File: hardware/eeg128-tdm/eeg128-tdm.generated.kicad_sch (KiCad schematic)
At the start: 640 parts, among them J1 0.5K-QX-32PWB, J10 S4B-PH-SM4-TB(LF)(SN), J11 S2B-PH-SM4-TB(LF)(SN), J2 0.5K-QX-32PWB, J3 0.5K-QX-32PWB, J4 0.5K-QX-32PWB, J5 0.5K-QX-32PWB, J6 0.5K-QX-32PWB, J7 0.5K-QX-32PWB, J8 0.5K-QX-32PWB, J9 TYPE-C-31-M-12, U1 CD74HC4067M96, U10 CD74HC4067M96, U11 CD74HC4067M96, U12 CD74HC4067M96, U13 CD74HC4067M96, U14 CD74HC4067M96, U15 CD74HC4067M96, U16 CD74HC4067M96, U17 TLV9064IPWR, U18 TLV9064IPWR, U19 TLV9064IPWR, U2 CD74HC4067M96, U20 TLV9064IPWR, U21 ADS131M08IPBSR, U22 OPA4171AIPWR, U23 RP2040, U24 TPS7A2033PDBVR, U25 AP2112K-3.3TRG1, U26 W25Q16JVSSIQ, U27 OT2JI-111-8.192M, U3 CD74HC4067M96, U4 CD74HC4067M96, U5 CD74HC4067M96, U6 CD74HC4067M96, U7 CD74HC4067M96, U8 CD74HC4067M96, U9 CD74HC4067M96, Y1 X322512MSB4SI

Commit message: Materialize generated KiCad schematic and release manifest
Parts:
- added R538: 0603WAF5101T5E, NBFM1_A0:R538, symbol NBFM1_A0:GEN_2_a2422ced9e0c
- added R539: 0603WAF5101T5E, NBFM1_A0:R539, symbol NBFM1_A0:GEN_2_a2422ced9e0c
- J9: symbol NBFM1_A0:GEN_18_30158393f200 -> NBFM1_A0:GEN_20_6661cee1473b
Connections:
- net DGND is gone; now on net AGND: C61.1 (Pin_1), C63.1 (Pin_1), C64.1 (Pin_1), U21.8 (Pin_8), U23.1 (Pin_1), U26.5 (Pin_5), U27.3 (Pin_3)
- net ISO_GND is gone; now on net AGND: J11.1 (Pin_1)
- net VCM_DIV_HI is gone; now on net 3V3A: R529.2 (Pin_2)
- net 3V3A: now also C1.2 (Pin_2), C10.2 (Pin_2), C11.2 (Pin_2), C12.2 (Pin_2), C13.2 (Pin_2), C14.2 (Pin_2), C15.2 (Pin_2), C16.2 (Pin_2), C18.2 (Pin_2), C2.2 (Pin_2), C21.2 (Pin_2), C22.2 (Pin_2), C23.2 (Pin_2), C24.2 (Pin_2), C25.2 (Pin_2), C26.2 (Pin_2), C27.2 (Pin_2), C28.2 (Pin_2), C29.2 (Pin_2), C3.2 (Pin_2), C30.2 (Pin_2), C31.2 (Pin_2), C32.2 (Pin_2), C33.2 (Pin_2), C34.2 (Pin_2), C35.2 (Pin_2), C36.2 (Pin_2), C37.2 (Pin_2), C38.2 (Pin_2), C39.2 (Pin_2), C4.2 (Pin_2), C40.2 (Pin_2), C41.2 (Pin_2), C5.2 (Pin_2), C6.2 (Pin_2), C7.2 (Pin_2), C8.2 (Pin_2), C9.2 (Pin_2), U24.1 (Pin_1)
- net 3V3D: now also C20.2 (Pin_2), C42.2 (Pin_2), C44.2 (Pin_2), C45.2 (Pin_2), C46.2 (Pin_2), C47.2 (Pin_2), C48.2 (Pin_2), C49.2 (Pin_2), C53.2 (Pin_2), C54.2 (Pin_2), C55.2 (Pin_2), C56.2 (Pin_2), C57.2 (Pin_2), C58.2 (Pin_2), C59.2 (Pin_2), C60.2 (Pin_2), U25.1 (Pin_1), U27.4 (Pin_4)
- net 5V_ISO: now also C17.2 (Pin_2), C19.2 (Pin_2), J9.A6 (Pin_A6), J9.B12 (Pin_B12), J9.B6 (Pin_B6), J9.S1 (Pin_S1), U24.3 (Pin_3), U24.5 (Pin_5), U25.3 (Pin_3), U25.5 (Pin_5)
- net ADC_REFIN: now also C43.2 (Pin_2)
- net AGND: now also C1.1 (Pin_1), C10.1 (Pin_1), C11.1 (Pin_1), C12.1 (Pin_1), C13.1 (Pin_1), C14.1 (Pin_1), C15.1 (Pin_1), C16.1 (Pin_1), C17.1 (Pin_1), C18.1 (Pin_1), C19.1 (Pin_1), C2.1 (Pin_1), C20.1 (Pin_1), C21.1 (Pin_1), C22.1 (Pin_1), C23.1 (Pin_1), C24.1 (Pin_1), C25.1 (Pin_1), C26.1 (Pin_1), C27.1 (Pin_1), C28.1 (Pin_1), C29.1 (Pin_1), C3.1 (Pin_1), C30.1 (Pin_1), C31.1 (Pin_1), C32.1 (Pin_1), C33.1 (Pin_1), C34.1 (Pin_1), C35.1 (Pin_1), C36.1 (Pin_1), C37.1 (Pin_1), C38.1 (Pin_1), C39.1 (Pin_1), C4.1 (Pin_1), C40.1 (Pin_1), C41.1 (Pin_1), C42.1 (Pin_1), C43.1 (Pin_1), C44.1 (Pin_1), C45.1 (Pin_1), C46.1 (Pin_1), C47.1 (Pin_1), C48.1 (Pin_1), C49.1 (Pin_1), C5.1 (Pin_1), C50.1 (Pin_1), C51.1 (Pin_1), C52.1 (Pin_1), C53.1 (Pin_1), C54.1 (Pin_1), C55.1 (Pin_1), C56.1 (Pin_1), C57.1 (Pin_1), C58.1 (Pin_1), C59.1 (Pin_1), C6.1 (Pin_1), C60.1 (Pin_1), C7.1 (Pin_1), C8.1 (Pin_1), C9.1 (Pin_1), J9.B4 (Pin_B4), J9.B5 (Pin_B5), J9.S1 (Pin_S1), U24.4 (Pin_4), U25.4 (Pin_4), Y1.1 (Pin_1), Y1.3 (Pin_3), R538.1 (Pin_1), R539.1 (Pin_1)
- net SHIELD: now also J9.A5 (Pin_A5)
- net USB_DM: now also J9.A8 (Pin_A8), J9.B8 (Pin_B8)
- net USB_DP: now also J9.A9 (Pin_A9), J9.B9 (Pin_B9)
- net VREG_1V1: now also C50.2 (Pin_2), C51.2 (Pin_2), C52.2 (Pin_2)
- new net USB_CC1: J9.S1 (Pin_S1), R538.2 (Pin_2)
- new net USB_CC2: J9.B1 (Pin_B1), R539.2 (Pin_2)
- no-connect marks 176 -> 32

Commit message: Materialize generated KiCad schematic and release manifest
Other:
- moved on the sheet: C10, C13, C14, C15, C18, C19, C20, C23, C24, C28, C29, C3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

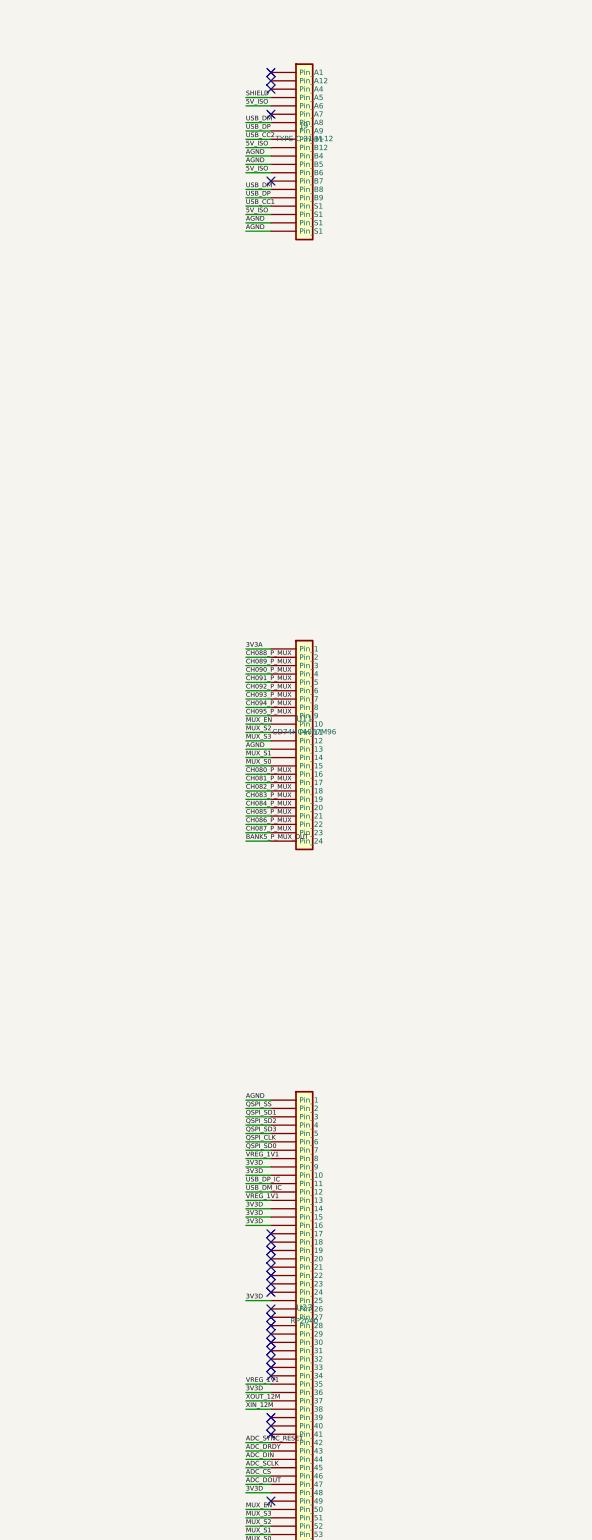
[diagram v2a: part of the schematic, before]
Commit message: Materialize generated KiCad schematic and release manifest
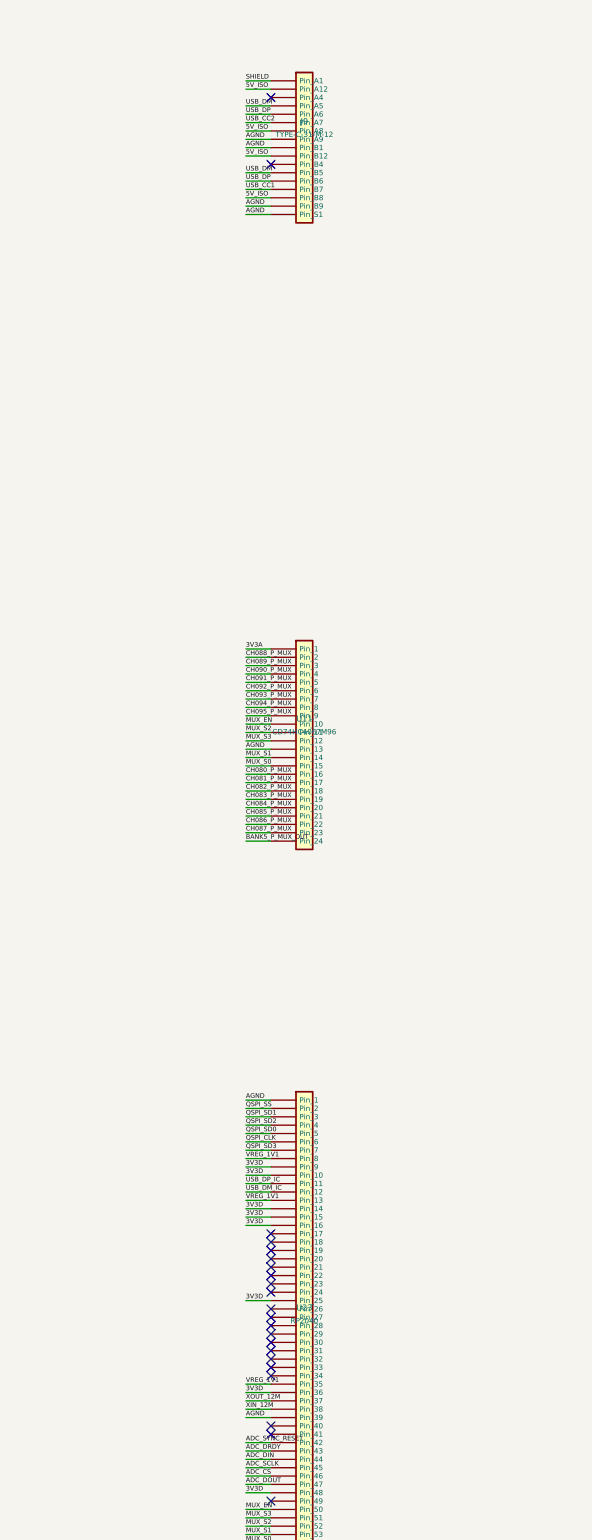
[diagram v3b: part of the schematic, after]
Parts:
- J9: symbol NBFM1_A0:GEN_20_6661cee1473b -> NBFM1_A0:GEN_17_9492c1d87d9b
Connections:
- net 5V_ISO: now also J9.A12 (Pin_A12), J9.A8 (Pin_A8), J9.B8 (Pin_B8); no longer J9.A6 (Pin_A6), J9.B6 (Pin_B6), J9.S1 (Pin_S1)
- net AGND: now also J9.A9 (Pin_A9), J9.B1 (Pin_B1), J9.B9 (Pin_B9), U23.39 (Pin_39); no longer J9.B4 (Pin_B4), J9.B5 (Pin_B5)
- net QSPI_SD0: now also U23.5 (Pin_5); no longer U23.7 (Pin_7)
- net QSPI_SD3: now also U23.7 (Pin_7); no longer U23.5 (Pin_5)
- net SHIELD: now also J9.A1 (Pin_A1); no longer J9.A5 (Pin_A5)
- net USB_CC1: now also J9.B7 (Pin_B7); no longer J9.S1 (Pin_S1)
- net USB_CC2: now also J9.A7 (Pin_A7); no longer J9.B1 (Pin_B1)
- net USB_DM: now also J9.A5 (Pin_A5), J9.B5 (Pin_B5); no longer J9.A8 (Pin_A8), J9.B8 (Pin_B8)
- net USB_DP: now also J9.A6 (Pin_A6), J9.B6 (Pin_B6); no longer J9.A9 (Pin_A9), J9.B9 (Pin_B9)
- no-connect marks 32 -> 28
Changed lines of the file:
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@@
   )
   (wire
-    (pts (xy 775.970 67.310) (xy 772.160 67.310))
-    (stroke (width 0) (type default))
-  )
-  (wire
-    (pts (xy 775.970 66.040) (xy 772.160 66.040))
-    (stroke (width 0) (type default))
-  )
-  (wire
     (pts (xy 775.970 64.770) (xy 772.160 64.770))
     (stroke (width 0) (type default))
@@
   )
   (wire
-    (pts (xy 775.970 58.420) (xy 772.160 58.420))
+    (pts (xy 775.970 59.690) (xy 772.160 59.690))
     (stroke (width 0) (type default))
   )
   (wire
-    (pts (xy 775.970 57.150) (xy 772.160 57.150))
+    (pts (xy 775.970 58.420) (xy 772.160 58.420))
     (stroke (width 0) (type default))
   )
@@
   )
   (wire
+    (pts (xy 775.970 49.530) (xy 772.160 49.530))
+    (stroke (width 0) (type default))
+  )
+  (wire
     (pts (xy 775.970 48.260) (xy 772.160 48.260))
     (stroke (width 0) (type default))
   )
   (wire
-    (pts (xy 775.970 46.990) (xy 772.160 46.990))
+    (pts (xy 775.970 45.720) (xy 772.160 45.720))
+    (stroke (width 0) (type default))
+  )
+  (wire
+    (pts (xy 775.970 44.450) (xy 772.160 44.450))
     (stroke (width 0) (type default))
   )
@@
   )
   (wire
+    (pts (xy 775.970 247.650) (xy 772.160 247.650))
+    (stroke (width 0) (type default))
+  )
+  (wire
     (pts (xy 775.970 246.380) (xy 772.160 246.380))
     (stroke (width 0) (type default))
@@
   )
   (label "AGND"
-    (at 772.160 67.310 0)
+    (at 772.160 64.770 0)
     (effects (font (size 0.7 0.7)) (justify left bottom))
   )
   (label "AGND"
-    (at 772.160 66.040 0)
+    (at 772.160 63.500 0)
     (effects (font (size 0.7 0.7)) (justify left bottom))
   )
   (label "5V_ISO"
-    (at 772.160 64.770 0)
+    (at 772.160 62.230 0)
     (effects (font (size 0.7 0.7)) (justify left bottom))
   )
   (label "USB_CC1"
-    (at 772.160 63.500 0)
+    (at 772.160 60.960 0)
     (effects (font (size 0.7 0.7)) (justify left bottom))
   )
   (label "USB_DP"
-    (at 772.160 62.230 0)
+    (at 772.160 59.690 0)
     (effects (font (size 0.7 0.7)) (justify left bottom))
   )
   (label "USB_DM"
-    (at 772.160 60.960 0)
+    (at 772.160 58.420 0)
     (effects (font (size 0.7 0.7)) (justify left bottom))
   )
   (label "5V_ISO"
-    (at 772.160 58.420 0)
+    (at 772.160 55.880 0)
     (effects (font (size 0.7 0.7)) (justify left bottom))
   )
   (label "AGND"
-    (at 772.160 57.150 0)
+    (at 772.160 54.610 0)
     (effects (font (size 0.7 0.7)) (justify left bottom))
   )
   (label "AGND"
-    (at 772.160 55.880 0)
+    (at 772.160 53.340 0)
     (effects (font (size 0.7 0.7)) (justify left bottom))
   )
   (label "5V_ISO"
-    (at 772.160 54.610 0)
+    (at 772.160 52.070 0)
     (effects (font (size 0.7 0.7)) (justify left bottom))
   )
   (label "USB_CC2"
-    (at 772.160 53.340 0)
+    (at 772.160 50.800 0)
     (effects (font (size 0.7 0.7)) (justify left bottom))
   )
   (label "USB_DP"
-    (at 772.160 52.070 0)
+    (at 772.160 49.530 0)
     (effects (font (size 0.7 0.7)) (justify left bottom))
   )
   (label "USB_DM"
-    (at 772.160 50.800 0)
+    (at 772.160 48.260 0)
     (effects (font (size 0.7 0.7)) (justify left bottom))
   )
   (label "5V_ISO"
-    (at 772.160 48.260 0)
+    (at 772.160 45.720 0)
     (effects (font (size 0.7 0.7)) (justify left bottom))
   )
   (label "SHIELD"
-    (at 772.160 46.990 0)
+    (at 772.160 44.450 0)
     (effects (font (size 0.7 0.7)) (justify left bottom))
   )
@@
     (effects (font (size 0.7 0.7)) (justify left bottom))
   )
+  (label "AGND"
+    (at 772.160 247.650 0)
+    (effects (font (size 0.7 0.7)) (justify left bottom))
+  )
   (label "XIN_12M"
     (at 772.160 246.380 0)
@@
     (effects (font (size 0.7 0.7)) (justify left bottom))
   )
-  (label "QSPI_SD0"
+  (label "QSPI_SD3"
     (at 772.160 207.010 0)
     (effects (font (size 0.7 0.7)) (justify left bottom))
@@
     (effects (font (size 0.7 0.7)) (justify left bottom))
   )
-  (label "QSPI_SD3"
+  (label "QSPI_SD0"
     (at 772.160 204.470 0)
     (effects (font (size 0.7 0.7)) (justify left bottom))
@@
     (effects (font (size 0.7 0.7)) (justify left bottom))
   )
-  (no_connect (at 775.970 59.690))
-  (no_connect (at 775.970 49.530))
-  (no_connect (at 775.970 45.720))
-  (no_connect (at 775.970 44.450))
-  (no_connect (at 775.970 43.180))
+  (no_connect (at 775.970 57.150))
+  (no_connect (at 775.970 46.990))
   (no_connect (at 591.820 228.600))
   (no_connect (at 591.820 222.250))
@@
   (no_connect (at 775.970 250.190))
   (no_connect (at 775.970 248.920))
-  (no_connect (at 775.970 247.650))
   (no_connect (at 775.970 241.300))
   (no_connect (at 775.970 240.030))
@@
   )
   (symbol
-    (lib_id "NBFM1_A0:GEN_20_6661cee1473b")
-    (at 781.050 55.245 0)
+    (lib_id "NBFM1_A0:GEN_17_9492c1d87d9b")
+    (at 781.050 54.610 0)
     (unit 1)
     (exclude_from_sim no)
@@
     (on_board yes)
     (dnp no)
-    (property "Reference" "J9" (at 781.050 51.245 0) (effects (font (size 0.9 0.9))))
-    (property "Value" "TYPE-C-31-M-12" (at 781.050 53.245 0) (effects (font (size 0.8 0.8))))
-    (property "Footprint" "NBFM1_A0:J9" (at 781.050 55.245 0) (effects (font (size 0.8 0.8)) (hide yes)))
-    (property "Datasheet" "" (at 781.050 55.245 0) (effects (font (size 0.8 0.8)) (hide yes)))
-    (property "Description" "Generated connectivity symbol; BOM footprint: USB-C-16P_RA" (at 781.050 55.245 0) (effects (font (size 0.8 0.8)) (hide yes)))
+    (property "Reference" "J9" (at 781.050 50.610 0) (effects (font (size 0.9 0.9))))
+    (property "Value" "TYPE-C-31-M-12" (at 781.050 52.610 0) (effects (font (size 0.8 0.8))))
+    (property "Footprint" "NBFM1_A0:J9" (at 781.050 54.610 0) (effects (font (size 0.8 0.8)) (hide yes)))
+    (property "Datasheet" "" (at 781.050 54.610 0) (effects (font (size 0.8 0.8)) (hide yes)))
+    (property "Description" "Generated connectivity symbol; BOM footprint: USB-C-16P_RA" (at 781.050 54.610 0) (effects (font (size 0.8 0.8)) (hide yes)))
     (pin "A1"
     )
@@
     )
     (pin "S1"
-    )
-    (pin "S1"
-    )
-    (pin "S1"
-    )
-    (pin "S1"

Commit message: Materialize generated KiCad schematic and release manifest
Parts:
- C1: footprint NBFM1_A0:C1 -> C1
- C10: footprint NBFM1_A0:C10 -> C10
- C11: footprint NBFM1_A0:C11 -> C11
- C12: footprint NBFM1_A0:C12 -> C12
- C13: footprint NBFM1_A0:C13 -> C13
- C14: footprint NBFM1_A0:C14 -> C14
- C15: footprint NBFM1_A0:C15 -> C15
- C16: footprint NBFM1_A0:C16 -> C16
- C17: footprint NBFM1_A0:C17 -> C17
- C18: footprint NBFM1_A0:C18 -> C18
- C19: footprint NBFM1_A0:C19 -> C19
- C2: footprint NBFM1_A0:C2 -> C2
- C20: footprint NBFM1_A0:C20 -> C20
- C21: footprint NBFM1_A0:C21 -> C21
- C22: footprint NBFM1_A0:C22 -> C22
- C23: footprint NBFM1_A0:C23 -> C23
- C24: footprint NBFM1_A0:C24 -> C24
- C25: footprint NBFM1_A0:C25 -> C25
- C26: footprint NBFM1_A0:C26 -> C26
- C27: footprint NBFM1_A0:C27 -> C27
- C28: footprint NBFM1_A0:C28 -> C28
- C29: footprint NBFM1_A0:C29 -> C29
- C3: footprint NBFM1_A0:C3 -> C3
- C30: footprint NBFM1_A0:C30 -> C30
- C31: footprint NBFM1_A0:C31 -> C31
- C32: footprint NBFM1_A0:C32 -> C32
- C33: footprint NBFM1_A0:C33 -> C33
- C34: footprint NBFM1_A0:C34 -> C34
- C35: footprint NBFM1_A0:C35 -> C35
- C36: footprint NBFM1_A0:C36 -> C36
- C37: footprint NBFM1_A0:C37 -> C37
- C38: footprint NBFM1_A0:C38 -> C38
- C39: footprint NBFM1_A0:C39 -> C39
- C4: footprint NBFM1_A0:C4 -> C4
- C40: footprint NBFM1_A0:C40 -> C40
- C41: footprint NBFM1_A0:C41 -> C41
- C42: footprint NBFM1_A0:C42 -> C42
- C43: footprint NBFM1_A0:C43 -> C43
- C44: footprint NBFM1_A0:C44 -> C44
- C45: footprint NBFM1_A0:C45 -> C45
- C46: footprint NBFM1_A0:C46 -> C46
- C47: footprint NBFM1_A0:C47 -> C47
- C48: footprint NBFM1_A0:C48 -> C48
- C49: footprint NBFM1_A0:C49 -> C49
- C5: footprint NBFM1_A0:C5 -> C5
- C50: footprint NBFM1_A0:C50 -> C50
- C51: footprint NBFM1_A0:C51 -> C51
- C52: footprint NBFM1_A0:C52 -> C52
- C53: footprint NBFM1_A0:C53 -> C53
- C54: footprint NBFM1_A0:C54 -> C54
- C55: footprint NBFM1_A0:C55 -> C55
- C56: footprint NBFM1_A0:C56 -> C56
- C57: footprint NBFM1_A0:C57 -> C57
- C58: footprint NBFM1_A0:C58 -> C58
- C59: footprint NBFM1_A0:C59 -> C59
- C6: footprint NBFM1_A0:C6 -> C6
- C60: footprint NBFM1_A0:C60 -> C60
- C61: footprint NBFM1_A0:C61 -> C61
- C62: footprint NBFM1_A0:C62 -> C62
- C63: footprint NBFM1_A0:C63 -> C63
- C64: footprint NBFM1_A0:C64 -> C64
- C7: footprint NBFM1_A0:C7 -> C7
- C8: footprint NBFM1_A0:C8 -> C8
- C9: footprint NBFM1_A0:C9 -> C9
- J1: footprint NBFM1_A0:J1 -> J1
- J10: footprint NBFM1_A0:J10 -> J10
- J11: footprint NBFM1_A0:J11 -> J11
- J2: footprint NBFM1_A0:J2 -> J2
- J3: footprint NBFM1_A0:J3 -> J3
- J4: footprint NBFM1_A0:J4 -> J4
- J5: footprint NBFM1_A0:J5 -> J5
- J6: footprint NBFM1_A0:J6 -> J6
- J7: footprint NBFM1_A0:J7 -> J7
- J8: footprint NBFM1_A0:J8 -> J8
- J9: footprint NBFM1_A0:J9 -> USB_C_Receptacle_HRO_TYPE-C-31-M-12
- R1: footprint NBFM1_A0:R1 -> R1
- R10: footprint NBFM1_A0:R10 -> R10
- R100: footprint NBFM1_A0:R100 -> R100
- R101: footprint NBFM1_A0:R101 -> R101
- R102: footprint NBFM1_A0:R102 -> R102
- R103: footprint NBFM1_A0:R103 -> R103
- R104: footprint NBFM1_A0:R104 -> R104
- R105: footprint NBFM1_A0:R105 -> R105
- R106: footprint NBFM1_A0:R106 -> R106
- R107: footprint NBFM1_A0:R107 -> R107
- R108: footprint NBFM1_A0:R108 -> R108
- R109: footprint NBFM1_A0:R109 -> R109
- R11: footprint NBFM1_A0:R11 -> R11
- R110: footprint NBFM1_A0:R110 -> R110
- R111: footprint NBFM1_A0:R111 -> R111
- R112: footprint NBFM1_A0:R112 -> R112
- R113: footprint NBFM1_A0:R113 -> R113
- R114: footprint NBFM1_A0:R114 -> R114
- R115: footprint NBFM1_A0:R115 -> R115
- R116: footprint NBFM1_A0:R116 -> R116
- R117: footprint NBFM1_A0:R117 -> R117
- R118: footprint NBFM1_A0:R118 -> R118
- R119: footprint NBFM1_A0:R119 -> R119
- R12: footprint NBFM1_A0:R12 -> R12
- R120: footprint NBFM1_A0:R120 -> R120
- R121: footprint NBFM1_A0:R121 -> R121
- R122: footprint NBFM1_A0:R122 -> R122
- R123: footprint NBFM1_A0:R123 -> R123
- R124: footprint NBFM1_A0:R124 -> R124
- R125: footprint NBFM1_A0:R125 -> R125
- R126: footprint NBFM1_A0:R126 -> R126
- R127: footprint NBFM1_A0:R127 -> R127
- R128: footprint NBFM1_A0:R128 -> R128
- R129: footprint NBFM1_A0:R129 -> R129
- R13: footprint NBFM1_A0:R13 -> R13
- R130: footprint NBFM1_A0:R130 -> R130
- R131: footprint NBFM1_A0:R131 -> R131
- R132: footprint NBFM1_A0:R132 -> R132
- R133: footprint NBFM1_A0:R133 -> R133
- R134: footprint NBFM1_A0:R134 -> R134
- R135: footprint NBFM1_A0:R135 -> R135
- R136: footprint NBFM1_A0:R136 -> R136
- R137: footprint NBFM1_A0:R137 -> R137
- R138: footprint NBFM1_A0:R138 -> R138
- R139: footprint NBFM1_A0:R139 -> R139
- R14: footprint NBFM1_A0:R14 -> R14
- R140: footprint NBFM1_A0:R140 -> R140
- R141: footprint NBFM1_A0:R141 -> R141
- R142: footprint NBFM1_A0:R142 -> R142
- R143: footprint NBFM1_A0:R143 -> R143
- R144: footprint NBFM1_A0:R144 -> R144
- R145: footprint NBFM1_A0:R145 -> R145
- R146: footprint NBFM1_A0:R146 -> R146
- R147: footprint NBFM1_A0:R147 -> R147
- R148: footprint NBFM1_A0:R148 -> R148
- R149: footprint NBFM1_A0:R149 -> R149
- R15: footprint NBFM1_A0:R15 -> R15
- R150: footprint NBFM1_A0:R150 -> R150
- R151: footprint NBFM1_A0:R151 -> R151
- R152: footprint NBFM1_A0:R152 -> R152
- R153: footprint NBFM1_A0:R153 -> R153
- R154: footprint NBFM1_A0:R154 -> R154
- R155: footprint NBFM1_A0:R155 -> R155
- R156: footprint NBFM1_A0:R156 -> R156
- R157: footprint NBFM1_A0:R157 -> R157
- R158: footprint NBFM1_A0:R158 -> R158
- R159: footprint NBFM1_A0:R159 -> R159
- R16: footprint NBFM1_A0:R16 -> R16
- R160: footprint NBFM1_A0:R160 -> R160
- R161: footprint NBFM1_A0:R161 -> R161
- R162: footprint NBFM1_A0:R162 -> R162
- R163: footprint NBFM1_A0:R163 -> R163
- R164: footprint NBFM1_A0:R164 -> R164
- R165: footprint NBFM1_A0:R165 -> R165
- R166: footprint NBFM1_A0:R166 -> R166
- R167: footprint NBFM1_A0:R167 -> R167
- R168: footprint NBFM1_A0:R168 -> R168
- R169: footprint NBFM1_A0:R169 -> R169
- R17: footprint NBFM1_A0:R17 -> R17
- R170: footprint NBFM1_A0:R170 -> R170
- R171: footprint NBFM1_A0:R171 -> R171
- R172: footprint NBFM1_A0:R172 -> R172
- R173: footprint NBFM1_A0:R173 -> R173
- R174: footprint NBFM1_A0:R174 -> R174
- R175: footprint NBFM1_A0:R175 -> R175
- R176: footprint NBFM1_A0:R176 -> R176
- R177: footprint NBFM1_A0:R177 -> R177
- R178: footprint NBFM1_A0:R178 -> R178
- R179: footprint NBFM1_A0:R179 -> R179
- R18: footprint NBFM1_A0:R18 -> R18
- R180: footprint NBFM1_A0:R180 -> R180
- R181: footprint NBFM1_A0:R181 -> R181
- R182: footprint NBFM1_A0:R182 -> R182
- R183: footprint NBFM1_A0:R183 -> R183
- R184: footprint NBFM1_A0:R184 -> R184
- R185: footprint NBFM1_A0:R185 -> R185
- R186: footprint NBFM1_A0:R186 -> R186
- R187: footprint NBFM1_A0:R187 -> R187
- R188: footprint NBFM1_A0:R188 -> R188
- R189: footprint NBFM1_A0:R189 -> R189
- R19: footprint NBFM1_A0:R19 -> R19
- R190: footprint NBFM1_A0:R190 -> R190
- R191: footprint NBFM1_A0:R191 -> R191
- R192: footprint NBFM1_A0:R192 -> R192
- R193: footprint NBFM1_A0:R193 -> R193
- R194: footprint NBFM1_A0:R194 -> R194
- R195: footprint NBFM1_A0:R195 -> R195
- R196: footprint NBFM1_A0:R196 -> R196
- R197: footprint NBFM1_A0:R197 -> R197
- R198: footprint NBFM1_A0:R198 -> R198
- R199: footprint NBFM1_A0:R199 -> R199
- R2: footprint NBFM1_A0:R2 -> R2
- R20: footprint NBFM1_A0:R20 -> R20
- R200: footprint NBFM1_A0:R200 -> R200
- R201: footprint NBFM1_A0:R201 -> R201
- R202: footprint NBFM1_A0:R202 -> R202
- R203: footprint NBFM1_A0:R203 -> R203
- R204: footprint NBFM1_A0:R204 -> R204
- R205: footprint NBFM1_A0:R205 -> R205
- R206: footprint NBFM1_A0:R206 -> R206
- R207: footprint NBFM1_A0:R207 -> R207
- R208: footprint NBFM1_A0:R208 -> R208
- R209: footprint NBFM1_A0:R209 -> R209
- R21: footprint NBFM1_A0:R21 -> R21
- R210: footprint NBFM1_A0:R210 -> R210
- R211: footprint NBFM1_A0:R211 -> R211
- R212: footprint NBFM1_A0:R212 -> R212
- R213: footprint NBFM1_A0:R213 -> R213
- R214: footprint NBFM1_A0:R214 -> R214
- R215: footprint NBFM1_A0:R215 -> R215
- R216: footprint NBFM1_A0:R216 -> R216
- R217: footprint NBFM1_A0:R217 -> R217
- R218: footprint NBFM1_A0:R218 -> R218
- R219: footprint NBFM1_A0:R219 -> R219
- R22: footprint NBFM1_A0:R22 -> R22
- R220: footprint NBFM1_A0:R220 -> R220
- R221: footprint NBFM1_A0:R221 -> R221
- R222: footprint NBFM1_A0:R222 -> R222
- R223: footprint NBFM1_A0:R223 -> R223
- R224: footprint NBFM1_A0:R224 -> R224
- R225: footprint NBFM1_A0:R225 -> R225
- R226: footprint NBFM1_A0:R226 -> R226
- R227: footprint NBFM1_A0:R227 -> R227
- R228: footprint NBFM1_A0:R228 -> R228
- R229: footprint NBFM1_A0:R229 -> R229
- R23: footprint NBFM1_A0:R23 -> R23
- R230: footprint NBFM1_A0:R230 -> R230
- R231: footprint NBFM1_A0:R231 -> R231
- R232: footprint NBFM1_A0:R232 -> R232
- R233: footprint NBFM1_A0:R233 -> R233
- R234: footprint NBFM1_A0:R234 -> R234
- R235: footprint NBFM1_A0:R235 -> R235
- R236: footprint NBFM1_A0:R236 -> R236
- R237: footprint NBFM1_A0:R237 -> R237
- R238: footprint NBFM1_A0:R238 -> R238
- R239: footprint NBFM1_A0:R239 -> R239
- R24: footprint NBFM1_A0:R24 -> R24
- R240: footprint NBFM1_A0:R240 -> R240
- R241: footprint NBFM1_A0:R241 -> R241
- R242: footprint NBFM1_A0:R242 -> R242
- R243: footprint NBFM1_A0:R243 -> R243
- R244: footprint NBFM1_A0:R244 -> R244
- R245: footprint NBFM1_A0:R245 -> R245
- R246: footprint NBFM1_A0:R246 -> R246
- R247: footprint NBFM1_A0:R247 -> R247
- R248: footprint NBFM1_A0:R248 -> R248
- R249: footprint NBFM1_A0:R249 -> R249
- R25: footprint NBFM1_A0:R25 -> R25
- R250: footprint NBFM1_A0:R250 -> R250
- R251: footprint NBFM1_A0:R251 -> R251
- R252: footprint NBFM1_A0:R252 -> R252
- R253: footprint NBFM1_A0:R253 -> R253
- R254: footprint NBFM1_A0:R254 -> R254
- R255: footprint NBFM1_A0:R255 -> R255
- R256: footprint NBFM1_A0:R256 -> R256
- R257: footprint NBFM1_A0:R257 -> R257
- R258: footprint NBFM1_A0:R258 -> R258
- R259: footprint NBFM1_A0:R259 -> R259
- R26: footprint NBFM1_A0:R26 -> R26
- R260: footprint NBFM1_A0:R260 -> R260
- R261: footprint NBFM1_A0:R261 -> R261
- R262: footprint NBFM1_A0:R262 -> R262
- R263: footprint NBFM1_A0:R263 -> R263
- R264: footprint NBFM1_A0:R264 -> R264
- R265: footprint NBFM1_A0:R265 -> R265
- R266: footprint NBFM1_A0:R266 -> R266
- R267: footprint NBFM1_A0:R267 -> R267
- R268: footprint NBFM1_A0:R268 -> R268
- R269: footprint NBFM1_A0:R269 -> R269
- R27: footprint NBFM1_A0:R27 -> R27
- R270: footprint NBFM1_A0:R270 -> R270
- R271: footprint NBFM1_A0:R271 -> R271
- R272: footprint NBFM1_A0:R272 -> R272
- R273: footprint NBFM1_A0:R273 -> R273
- R274: footprint NBFM1_A0:R274 -> R274
- R275: footprint NBFM1_A0:R275 -> R275
- R276: footprint NBFM1_A0:R276 -> R276
- R277: footprint NBFM1_A0:R277 -> R277
- R278: footprint NBFM1_A0:R278 -> R278
- R279: footprint NBFM1_A0:R279 -> R279
- R28: footprint NBFM1_A0:R28 -> R28
- R280: footprint NBFM1_A0:R280 -> R280
- R281: footprint NBFM1_A0:R281 -> R281
- R282: footprint NBFM1_A0:R282 -> R282
- R283: footprint NBFM1_A0:R283 -> R283
- R284: footprint NBFM1_A0:R284 -> R284
- R285: footprint NBFM1_A0:R285 -> R285
- R286: footprint NBFM1_A0:R286 -> R286
- R287: footprint NBFM1_A0:R287 -> R287
- R288: footprint NBFM1_A0:R288 -> R288
- R289: footprint NBFM1_A0:R289 -> R289
- R29: footprint NBFM1_A0:R29 -> R29
- R290: footprint NBFM1_A0:R290 -> R290
- R291: footprint NBFM1_A0:R291 -> R291
- R292: footprint NBFM1_A0:R292 -> R292
- R293: footprint NBFM1_A0:R293 -> R293
- R294: footprint NBFM1_A0:R294 -> R294
- R295: footprint NBFM1_A0:R295 -> R295
- R296: footprint NBFM1_A0:R296 -> R296
- R297: footprint NBFM1_A0:R297 -> R297
- R298: footprint NBFM1_A0:R298 -> R298
- R299: footprint NBFM1_A0:R299 -> R299
- R3: footprint NBFM1_A0:R3 -> R3
- R30: footprint NBFM1_A0:R30 -> R30
- R300: footprint NBFM1_A0:R300 -> R300
- R301: footprint NBFM1_A0:R301 -> R301
- R302: footprint NBFM1_A0:R302 -> R302
- R303: footprint NBFM1_A0:R303 -> R303
- R304: footprint NBFM1_A0:R304 -> R304
- R305: footprint NBFM1_A0:R305 -> R305
- R306: footprint NBFM1_A0:R306 -> R306
- R307: footprint NBFM1_A0:R307 -> R307
- R308: footprint NBFM1_A0:R308 -> R308
- R309: footprint NBFM1_A0:R309 -> R309
- R31: footprint NBFM1_A0:R31 -> R31
- R310: footprint NBFM1_A0:R310 -> R310
- R311: footprint NBFM1_A0:R311 -> R311
- R312: footprint NBFM1_A0:R312 -> R312
- R313: footprint NBFM1_A0:R313 -> R313
- R314: footprint NBFM1_A0:R314 -> R314
- R315: footprint NBFM1_A0:R315 -> R315
- R316: footprint NBFM1_A0:R316 -> R316
- R317: footprint NBFM1_A0:R317 -> R317
- R318: footprint NBFM1_A0:R318 -> R318
- R319: footprint NBFM1_A0:R319 -> R319
- R32: footprint NBFM1_A0:R32 -> R32
- R320: footprint NBFM1_A0:R320 -> R320
- R321: footprint NBFM1_A0:R321 -> R321
- R322: footprint NBFM1_A0:R322 -> R322
- R323: footprint NBFM1_A0:R323 -> R323
- R324: footprint NBFM1_A0:R324 -> R324
- R325: footprint NBFM1_A0:R325 -> R325
- R326: footprint NBFM1_A0:R326 -> R326
- R327: footprint NBFM1_A0:R327 -> R327
- R328: footprint NBFM1_A0:R328 -> R328
- R329: footprint NBFM1_A0:R329 -> R329
- R33: footprint NBFM1_A0:R33 -> R33
- R330: footprint NBFM1_A0:R330 -> R330
- R331: footprint NBFM1_A0:R331 -> R331
- R332: footprint NBFM1_A0:R332 -> R332
- R333: footprint NBFM1_A0:R333 -> R333
- R334: footprint NBFM1_A0:R334 -> R334
- R335: footprint NBFM1_A0:R335 -> R335
- R336: footprint NBFM1_A0:R336 -> R336
- R337: footprint NBFM1_A0:R337 -> R337
- R338: footprint NBFM1_A0:R338 -> R338
- R339: footprint NBFM1_A0:R339 -> R339
- R34: footprint NBFM1_A0:R34 -> R34
- R340: footprint NBFM1_A0:R340 -> R340
- R341: footprint NBFM1_A0:R341 -> R341
- R342: footprint NBFM1_A0:R342 -> R342
- R343: footprint NBFM1_A0:R343 -> R343
- R344: footprint NBFM1_A0:R344 -> R344
- R345: footprint NBFM1_A0:R345 -> R345
- R346: footprint NBFM1_A0:R346 -> R346
- R347: footprint NBFM1_A0:R347 -> R347
- R348: footprint NBFM1_A0:R348 -> R348
- R349: footprint NBFM1_A0:R349 -> R349
- R35: footprint NBFM1_A0:R35 -> R35
- R350: footprint NBFM1_A0:R350 -> R350
- R351: footprint NBFM1_A0:R351 -> R351
- R352: footprint NBFM1_A0:R352 -> R352
- R353: footprint NBFM1_A0:R353 -> R353
- R354: footprint NBFM1_A0:R354 -> R354
- R355: footprint NBFM1_A0:R355 -> R355
- R356: footprint NBFM1_A0:R356 -> R356
- R357: footprint NBFM1_A0:R357 -> R357
- R358: footprint NBFM1_A0:R358 -> R358
- R359: footprint NBFM1_A0:R359 -> R359
- R36: footprint NBFM1_A0:R36 -> R36
- R360: footprint NBFM1_A0:R360 -> R360
- R361: footprint NBFM1_A0:R361 -> R361
- R362: footprint NBFM1_A0:R362 -> R362
- R363: footprint NBFM1_A0:R363 -> R363
- R364: footprint NBFM1_A0:R364 -> R364
- R365: footprint NBFM1_A0:R365 -> R365
- R366: footprint NBFM1_A0:R366 -> R366
- R367: footprint NBFM1_A0:R367 -> R367
- R368: footprint NBFM1_A0:R368 -> R368
- R369: footprint NBFM1_A0:R369 -> R369
- R37: footprint NBFM1_A0:R37 -> R37
- R370: footprint NBFM1_A0:R370 -> R370
- R371: footprint NBFM1_A0:R371 -> R371
- R372: footprint NBFM1_A0:R372 -> R372
- R373: footprint NBFM1_A0:R373 -> R373
- R374: footprint NBFM1_A0:R374 -> R374
- R375: footprint NBFM1_A0:R375 -> R375
- R376: footprint NBFM1_A0:R376 -> R376
- R377: footprint NBFM1_A0:R377 -> R377
- R378: footprint NBFM1_A0:R378 -> R378
- R379: footprint NBFM1_A0:R379 -> R379
- R38: footprint NBFM1_A0:R38 -> R38
- R380: footprint NBFM1_A0:R380 -> R380
- R381: footprint NBFM1_A0:R381 -> R381
- R382: footprint NBFM1_A0:R382 -> R382
- R383: footprint NBFM1_A0:R383 -> R383
- R384: footprint NBFM1_A0:R384 -> R384
- R385: footprint NBFM1_A0:R385 -> R385
- R386: footprint NBFM1_A0:R386 -> R386
- R387: footprint NBFM1_A0:R387 -> R387
- R388: footprint NBFM1_A0:R388 -> R388
- R389: footprint NBFM1_A0:R389 -> R389
- R39: footprint NBFM1_A0:R39 -> R39
- R390: footprint NBFM1_A0:R390 -> R390
- R391: footprint NBFM1_A0:R391 -> R391
- R392: footprint NBFM1_A0:R392 -> R392
- R393: footprint NBFM1_A0:R393 -> R393
- R394: footprint NBFM1_A0:R394 -> R394
- R395: footprint NBFM1_A0:R395 -> R395
- R396: footprint NBFM1_A0:R396 -> R396
- R397: footprint NBFM1_A0:R397 -> R397
- R398: footprint NBFM1_A0:R398 -> R398
- R399: footprint NBFM1_A0:R399 -> R399
- R4: footprint NBFM1_A0:R4 -> R4
- R40: footprint NBFM1_A0:R40 -> R40
- R400: footprint NBFM1_A0:R400 -> R400
- R401: footprint NBFM1_A0:R401 -> R401
- R402: footprint NBFM1_A0:R402 -> R402
- R403: footprint NBFM1_A0:R403 -> R403
- R404: footprint NBFM1_A0:R404 -> R404
- R405: footprint NBFM1_A0:R405 -> R405
- R406: footprint NBFM1_A0:R406 -> R406
- R407: footprint NBFM1_A0:R407 -> R407
- R408: footprint NBFM1_A0:R408 -> R408
- R409: footprint NBFM1_A0:R409 -> R409
- R41: footprint NBFM1_A0:R41 -> R41
- R410: footprint NBFM1_A0:R410 -> R410
- R411: footprint NBFM1_A0:R411 -> R411
- R412: footprint NBFM1_A0:R412 -> R412
- R413: footprint NBFM1_A0:R413 -> R413
- R414: footprint NBFM1_A0:R414 -> R414
- R415: footprint NBFM1_A0:R415 -> R415
- R416: footprint NBFM1_A0:R416 -> R416
- R417: footprint NBFM1_A0:R417 -> R417
- R418: footprint NBFM1_A0:R418 -> R418
- R419: footprint NBFM1_A0:R419 -> R419
- R42: footprint NBFM1_A0:R42 -> R42
- R420: footprint NBFM1_A0:R420 -> R420
- R421: footprint NBFM1_A0:R421 -> R421
- R422: footprint NBFM1_A0:R422 -> R422
- R423: footprint NBFM1_A0:R423 -> R423
- R424: footprint NBFM1_A0:R424 -> R424
- R425: footprint NBFM1_A0:R425 -> R425
- R426: footprint NBFM1_A0:R426 -> R426
- R427: footprint NBFM1_A0:R427 -> R427
- R428: footprint NBFM1_A0:R428 -> R428
- R429: footprint NBFM1_A0:R429 -> R429
- R43: footprint NBFM1_A0:R43 -> R43
- R430: footprint NBFM1_A0:R430 -> R430
- R431: footprint NBFM1_A0:R431 -> R431
- R432: footprint NBFM1_A0:R432 -> R432
- R433: footprint NBFM1_A0:R433 -> R433
- R434: footprint NBFM1_A0:R434 -> R434
- R435: footprint NBFM1_A0:R435 -> R435
- R436: footprint NBFM1_A0:R436 -> R436
- R437: footprint NBFM1_A0:R437 -> R437
- R438: footprint NBFM1_A0:R438 -> R438
- R439: footprint NBFM1_A0:R439 -> R439
- R44: footprint NBFM1_A0:R44 -> R44
- R440: footprint NBFM1_A0:R440 -> R440
- R441: footprint NBFM1_A0:R441 -> R441
- R442: footprint NBFM1_A0:R442 -> R442
- R443: footprint NBFM1_A0:R443 -> R443
- R444: footprint NBFM1_A0:R444 -> R444
- R445: footprint NBFM1_A0:R445 -> R445
- R446: footprint NBFM1_A0:R446 -> R446
- R447: footprint NBFM1_A0:R447 -> R447
- R448: footprint NBFM1_A0:R448 -> R448
- R449: footprint NBFM1_A0:R449 -> R449
- R45: footprint NBFM1_A0:R45 -> R45
- R450: footprint NBFM1_A0:R450 -> R450
- R451: footprint NBFM1_A0:R451 -> R451
- R452: footprint NBFM1_A0:R452 -> R452
- R453: footprint NBFM1_A0:R453 -> R453
- R454: footprint NBFM1_A0:R454 -> R454
- R455: footprint NBFM1_A0:R455 -> R455
- R456: footprint NBFM1_A0:R456 -> R456
- R457: footprint NBFM1_A0:R457 -> R457
- R458: footprint NBFM1_A0:R458 -> R458
- R459: footprint NBFM1_A0:R459 -> R459
- R46: footprint NBFM1_A0:R46 -> R46
- R460: footprint NBFM1_A0:R460 -> R460
- R461: footprint NBFM1_A0:R461 -> R461
- R462: footprint NBFM1_A0:R462 -> R462
- R463: footprint NBFM1_A0:R463 -> R463
- R464: footprint NBFM1_A0:R464 -> R464
- R465: footprint NBFM1_A0:R465 -> R465
- R466: footprint NBFM1_A0:R466 -> R466
- R467: footprint NBFM1_A0:R467 -> R467
- R468: footprint NBFM1_A0:R468 -> R468
- R469: footprint NBFM1_A0:R469 -> R469
- R47: footprint NBFM1_A0:R47 -> R47
- R470: footprint NBFM1_A0:R470 -> R470
- R471: footprint NBFM1_A0:R471 -> R471
- R472: footprint NBFM1_A0:R472 -> R472
- R473: footprint NBFM1_A0:R473 -> R473
- R474: footprint NBFM1_A0:R474 -> R474
- R475: footprint NBFM1_A0:R475 -> R475
- R476: footprint NBFM1_A0:R476 -> R476
- R477: footprint NBFM1_A0:R477 -> R477
- R478: footprint NBFM1_A0:R478 -> R478
- R479: footprint NBFM1_A0:R479 -> R479
- R48: footprint NBFM1_A0:R48 -> R48
- R480: footprint NBFM1_A0:R480 -> R480
- R481: footprint NBFM1_A0:R481 -> R481
- R482: footprint NBFM1_A0:R482 -> R482
- R483: footprint NBFM1_A0:R483 -> R483
- R484: footprint NBFM1_A0:R484 -> R484
- R485: footprint NBFM1_A0:R485 -> R485
- R486: footprint NBFM1_A0:R486 -> R486
- R487: footprint NBFM1_A0:R487 -> R487
- R488: footprint NBFM1_A0:R488 -> R488
- R489: footprint NBFM1_A0:R489 -> R489
- R49: footprint NBFM1_A0:R49 -> R49
- R490: footprint NBFM1_A0:R490 -> R490
- R491: footprint NBFM1_A0:R491 -> R491
- R492: footprint NBFM1_A0:R492 -> R492
- R493: footprint NBFM1_A0:R493 -> R493
- R494: footprint NBFM1_A0:R494 -> R494
- R495: footprint NBFM1_A0:R495 -> R495
- R496: footprint NBFM1_A0:R496 -> R496
- R497: footprint NBFM1_A0:R497 -> R497
- R498: footprint NBFM1_A0:R498 -> R498
- R499: footprint NBFM1_A0:R499 -> R499
- R5: footprint NBFM1_A0:R5 -> R5
- R50: footprint NBFM1_A0:R50 -> R50
- R500: footprint NBFM1_A0:R500 -> R500
- R501: footprint NBFM1_A0:R501 -> R501
- R502: footprint NBFM1_A0:R502 -> R502
- R503: footprint NBFM1_A0:R503 -> R503
- R504: footprint NBFM1_A0:R504 -> R504
- R505: footprint NBFM1_A0:R505 -> R505
- R506: footprint NBFM1_A0:R506 -> R506
- R507: footprint NBFM1_A0:R507 -> R507
- R508: footprint NBFM1_A0:R508 -> R508
- R509: footprint NBFM1_A0:R509 -> R509
- R51: footprint NBFM1_A0:R51 -> R51
- R510: footprint NBFM1_A0:R510 -> R510
- R511: footprint NBFM1_A0:R511 -> R511
- R512: footprint NBFM1_A0:R512 -> R512
- R513: footprint NBFM1_A0:R513 -> R513
- R514: footprint NBFM1_A0:R514 -> R514
- R515: footprint NBFM1_A0:R515 -> R515
- R516: footprint NBFM1_A0:R516 -> R516
- R517: footprint NBFM1_A0:R517 -> R517
- R518: footprint NBFM1_A0:R518 -> R518
- R519: footprint NBFM1_A0:R519 -> R519
- R52: footprint NBFM1_A0:R52 -> R52
- R520: footprint NBFM1_A0:R520 -> R520
- R521: footprint NBFM1_A0:R521 -> R521
- R522: footprint NBFM1_A0:R522 -> R522
- R523: footprint NBFM1_A0:R523 -> R523
- R524: footprint NBFM1_A0:R524 -> R524
- R525: footprint NBFM1_A0:R525 -> R525
- R526: footprint NBFM1_A0:R526 -> R526
- R527: footprint NBFM1_A0:R527 -> R527
- R528: footprint NBFM1_A0:R528 -> R528
- R529: footprint NBFM1_A0:R529 -> R529
- R53: footprint NBFM1_A0:R53 -> R53
- R530: footprint NBFM1_A0:R530 -> R530
- R531: footprint NBFM1_A0:R531 -> R531
- R532: footprint NBFM1_A0:R532 -> R532
- R533: footprint NBFM1_A0:R533 -> R533
- R534: footprint NBFM1_A0:R534 -> R534
- R535: footprint NBFM1_A0:R535 -> R535
- R536: footprint NBFM1_A0:R536 -> R536
- R537: footprint NBFM1_A0:R537 -> R537
- R538: footprint NBFM1_A0:R538 -> R_0603_1608Metric
- R539: footprint NBFM1_A0:R539 -> R_0603_1608Metric
- R54: footprint NBFM1_A0:R54 -> R54
- R55: footprint NBFM1_A0:R55 -> R55
- R56: footprint NBFM1_A0:R56 -> R56
- R57: footprint NBFM1_A0:R57 -> R57
- R58: footprint NBFM1_A0:R58 -> R58
- R59: footprint NBFM1_A0:R59 -> R59
- R6: footprint NBFM1_A0:R6 -> R6
- R60: footprint NBFM1_A0:R60 -> R60
- R61: footprint NBFM1_A0:R61 -> R61
- R62: footprint NBFM1_A0:R62 -> R62
- R63: footprint NBFM1_A0:R63 -> R63
- R64: footprint NBFM1_A0:R64 -> R64
- R65: footprint NBFM1_A0:R65 -> R65
- R66: footprint NBFM1_A0:R66 -> R66
- R67: footprint NBFM1_A0:R67 -> R67
- R68: footprint NBFM1_A0:R68 -> R68
- R69: footprint NBFM1_A0:R69 -> R69
- R7: footprint NBFM1_A0:R7 -> R7
- R70: footprint NBFM1_A0:R70 -> R70
- R71: footprint NBFM1_A0:R71 -> R71
- R72: footprint NBFM1_A0:R72 -> R72
- R73: footprint NBFM1_A0:R73 -> R73
- R74: footprint NBFM1_A0:R74 -> R74
- R75: footprint NBFM1_A0:R75 -> R75
- R76: footprint NBFM1_A0:R76 -> R76
- R77: footprint NBFM1_A0:R77 -> R77
- R78: footprint NBFM1_A0:R78 -> R78
- R79: footprint NBFM1_A0:R79 -> R79
- R8: footprint NBFM1_A0:R8 -> R8
- R80: footprint NBFM1_A0:R80 -> R80
- R81: footprint NBFM1_A0:R81 -> R81
- R82: footprint NBFM1_A0:R82 -> R82
- R83: footprint NBFM1_A0:R83 -> R83
- R84: footprint NBFM1_A0:R84 -> R84
- R85: footprint NBFM1_A0:R85 -> R85
- R86: footprint NBFM1_A0:R86 -> R86
- R87: footprint NBFM1_A0:R87 -> R87
- R88: footprint NBFM1_A0:R88 -> R88
- R89: footprint NBFM1_A0:R89 -> R89
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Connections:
- net 3V3A: now also C1.1 (Pin_1), C10.1 (Pin_1), C11.1 (Pin_1), C12.1 (Pin_1), C13.1 (Pin_1), C14.1 (Pin_1), C15.1 (Pin_1), C16.1 (Pin_1), C18.1 (Pin_1), C2.1 (Pin_1), C21.1 (Pin_1), C22.1 (Pin_1)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; no longer C1.2 (Pin_2), C10.2 (Pin_2), C11.2 (Pin_2), C12.2 (Pin_2), C13.2 (Pin_2), C14.2 (Pin_2), C15.2 (Pin_2), C16.2 (Pin_2), C18.2 (Pin_2), C2.2 (Pin_2), C21.2 (Pin_2), C22.2 (Pin_2)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
- net 3V3D: now also C20.1 (Pin_1), C42.1 (Pin_1), C44.1 (Pin_1), C45.1 (Pin_1), C46.1 (Pin_1), C47.1 (Pin_1), C48.1 (Pin_1), C49.1 (Pin_1), C53.1 (Pin_1), C54.1 (Pin_1), C55.1 (Pin_1), C56.1 (Pin_1)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; no longer C20.2 (Pin_2), C42.2 (Pin_2), C44.2 (Pin_2), C45.2 (Pin_2), C46.2 (Pin_2), C47.2 (Pin_2), C48.2 (Pin_2), C49.2 (Pin_2), C53.2 (Pin_2), C54.2 (Pin_2), C55.2 (Pin_2), C56.2 (Pin_2)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
- net 5V_ISO: now also C17.1 (Pin_1), C19.1 (Pin_1), J11.1 (Pin_1), J9.A4 (Pin_A4), J9.A9 (Pin_A9), J9.B4 (Pin_B4), J9.B9 (Pin_B9), U24.1 (Pin_1), U25.1 (Pin_1); no longer C17.2 (Pin_2), C19.2 (Pin_2), J11.2 (Pin_2), J9.A12 (Pin_A12), J9.A8 (Pin_A8), J9.B12 (Pin_B12), J9.B8 (Pin_B8), U24.5 (Pin_5), U25.5 (Pin_5)
- net ADC0_N: now also R514.2 (Pin_2), U21.30 (Pin_30); no longer R514.1 (Pin_1), U21.3 (Pin_3)
- net ADC0_P: now also R513.2 (Pin_2), U21.29 (Pin_29); no longer R513.1 (Pin_1), U21.4 (Pin_4)
- net ADC1_N: now also R516.2 (Pin_2), U21.31 (Pin_31); no longer R516.1 (Pin_1), U21.2 (Pin_2)
- net ADC1_P: now also R515.2 (Pin_2), U21.32 (Pin_32); no longer R515.1 (Pin_1), U21.1 (Pin_1)
- net ADC2_N: now also R518.2 (Pin_2), U21.2 (Pin_2); no longer R518.1 (Pin_1), U21.31 (Pin_31)
- net ADC2_P: now also R517.2 (Pin_2), U21.1 (Pin_1); no longer R517.1 (Pin_1), U21.32 (Pin_32)
- net ADC3_N: now also R520.2 (Pin_2), U21.3 (Pin_3); no longer R520.1 (Pin_1), U21.30 (Pin_30)
- net ADC3_P: now also R519.2 (Pin_2), U21.4 (Pin_4); no longer R519.1 (Pin_1), U21.29 (Pin_29)
- net ADC4_N: now also R522.2 (Pin_2), U21.6 (Pin_6); no longer R522.1 (Pin_1), U21.27 (Pin_27)
- net ADC4_P: now also R521.2 (Pin_2), U21.5 (Pin_5); no longer R521.1 (Pin_1), U21.28 (Pin_28)
- net ADC5_N: now also R524.2 (Pin_2), U21.7 (Pin_7); no longer R524.1 (Pin_1), U21.26 (Pin_26)
- net ADC5_P: now also R523.2 (Pin_2), U21.8 (Pin_8); no longer R523.1 (Pin_1), U21.25 (Pin_25)
- net ADC6_N: now also R526.2 (Pin_2), U21.10 (Pin_10); no longer R526.1 (Pin_1), U21.23 (Pin_23)
- net ADC6_P: now also R525.2 (Pin_2), U21.9 (Pin_9); no longer R525.1 (Pin_1), U21.24 (Pin_24)
- net ADC7_N: now also R528.2 (Pin_2), U21.11 (Pin_11); no longer R528.1 (Pin_1), U21.22 (Pin_22)
- net ADC7_P: now also R527.2 (Pin_2), U21.12 (Pin_12); no longer R527.1 (Pin_1), U21.21 (Pin_21)
- net ADC_CLKIN: now also U21.23 (Pin_23), U27.3 (Pin_3); no longer U21.10 (Pin_10), U27.2 (Pin_2)
- net ADC_CS: now also U21.17 (Pin_17), U23.12 (Pin_12); no longer U21.16 (Pin_16), U23.46 (Pin_46)
- net ADC_DIN: now also U21.21 (Pin_21), U23.14 (Pin_14); no longer U21.12 (Pin_12), U23.44 (Pin_44)
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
